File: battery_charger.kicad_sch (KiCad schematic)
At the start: 1 part, among them J8 Conn_01x04

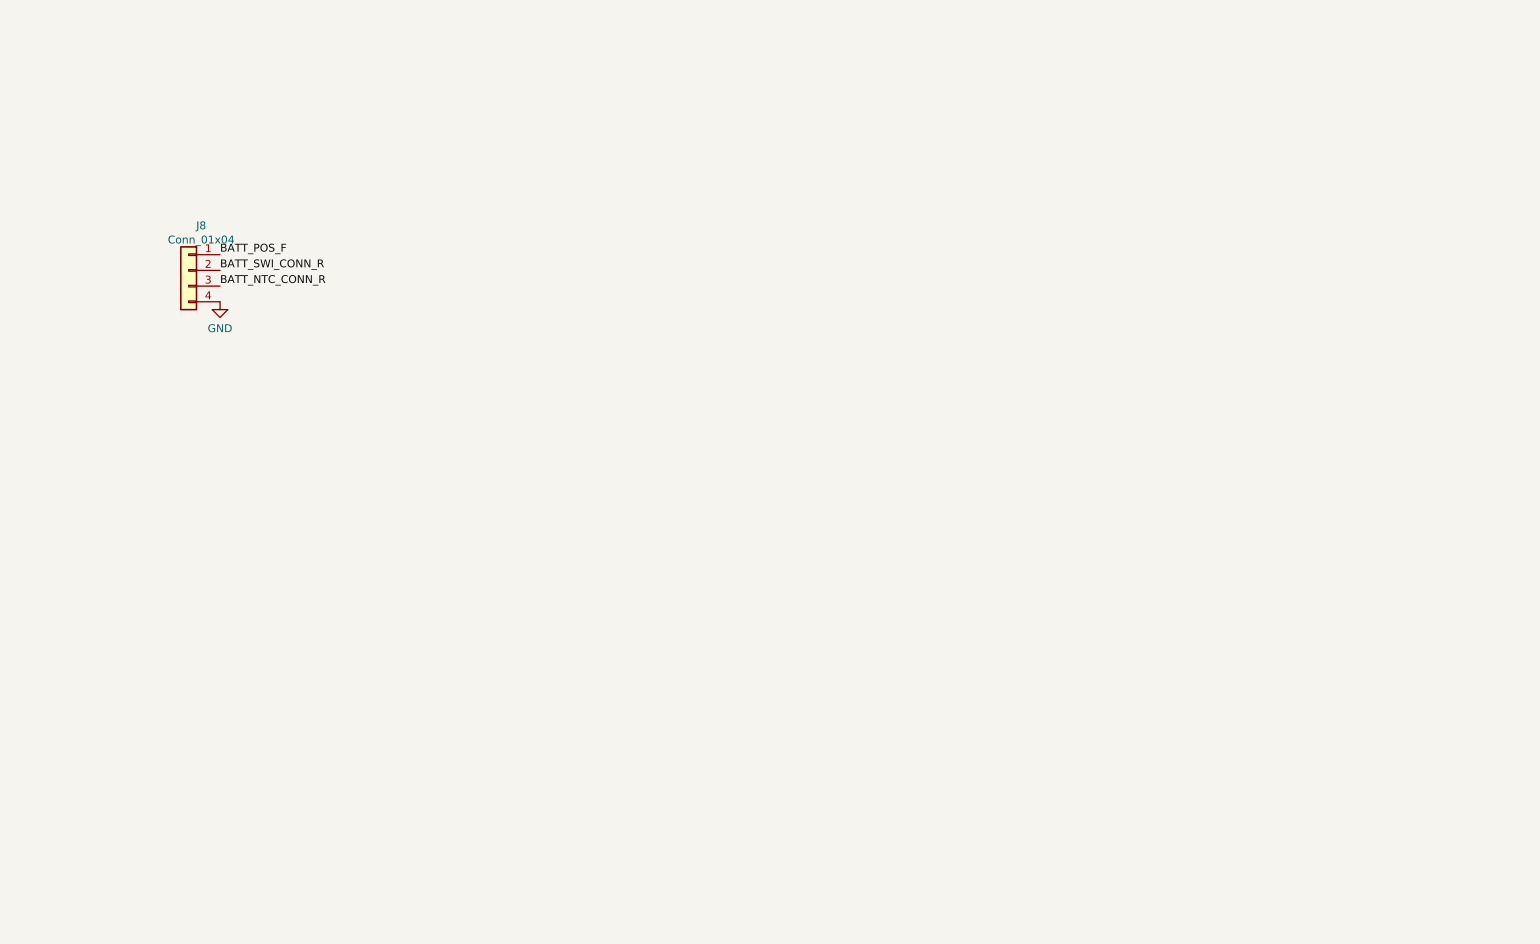
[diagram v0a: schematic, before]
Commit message: Add pinouts for dock connector; rearrange LCD backlight driver; copy the bq25895 schematic from SuperPower-RPi and add schottky to support 3.1A output on PMID.
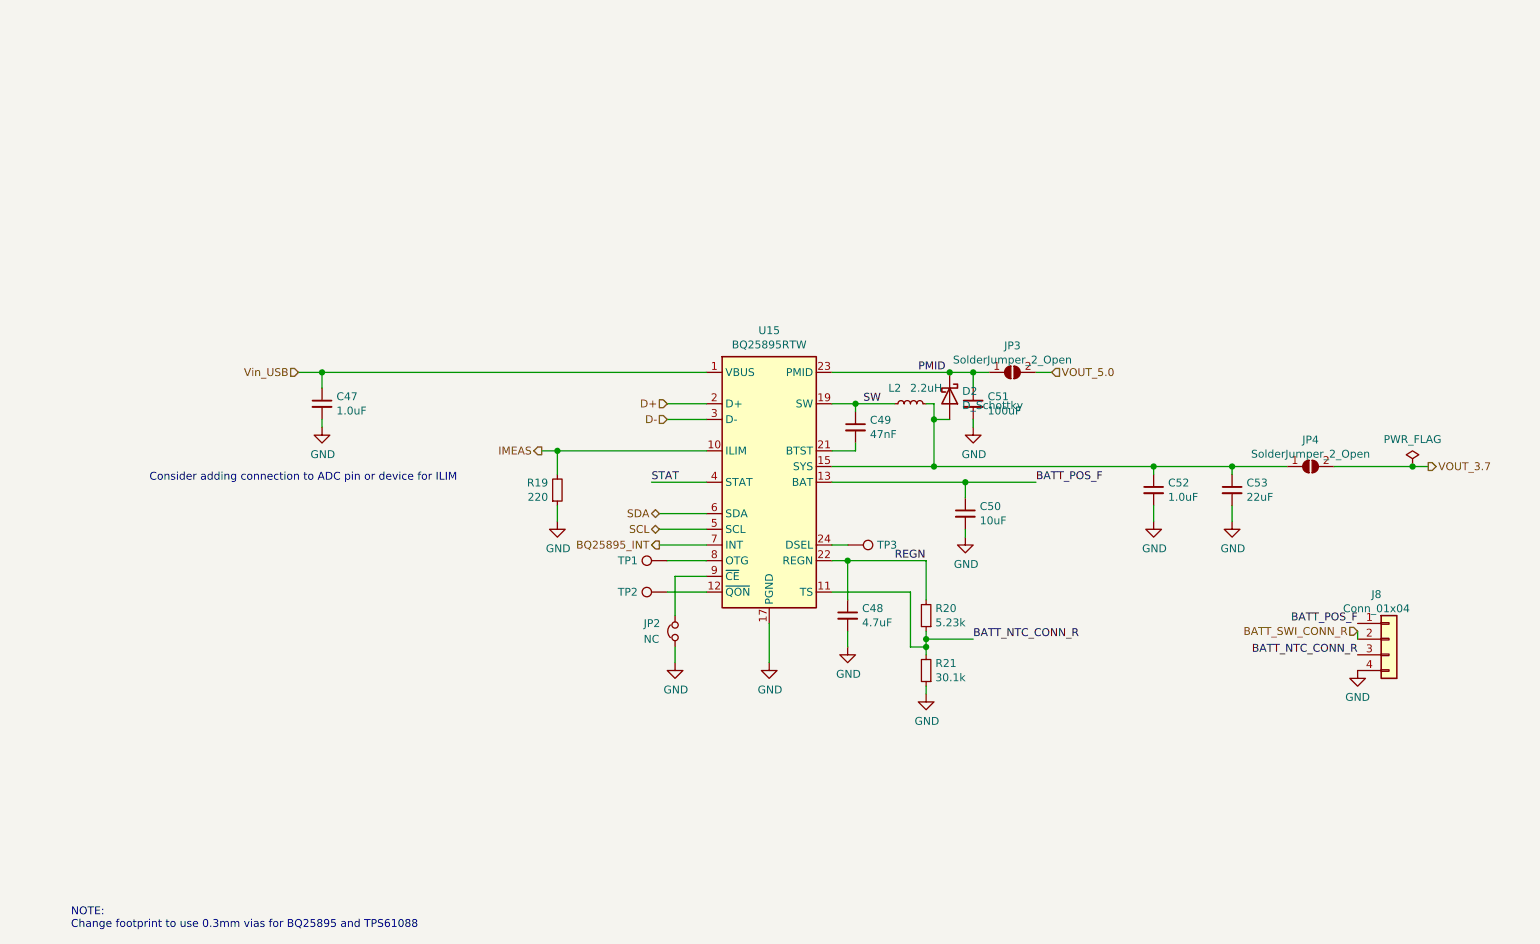
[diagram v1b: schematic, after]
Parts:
- added C47, C52: 1.0uF, Capacitor_SMD:C_0402_1005Metric, symbol Device:C_Small
- added C48: 4.7uF, Capacitor_SMD:C_0603_1608Metric, symbol Device:C_Small
- added C49: 47nF, Capacitor_SMD:C_0402_1005Metric, symbol Device:C_Small
- added C50: 10uF, Capacitor_SMD:C_0603_1608Metric, symbol Device:C_Small
- added C51: 100uF, Capacitor_SMD:C_1206_3216Metric, symbol Device:C_Small
- added C53: 22uF, Capacitor_SMD:C_0805_2012Metric, symbol Device:C_Small
- added D2: D_Schottky, footprints:NSR10F20NXT5G, symbol Device:D_Schottky
- added JP2: NC, Jumper:SolderJumper-2_P1.3mm_Bridged_RoundedPad1.0x1.5mm, symbol Device:Jumper_NC_Small
- added JP3, JP4: SolderJumper_2_Open, Jumper:SolderJumper-2_P1.3mm_Open_Pad1.0x1.5mm, symbol Jumper:SolderJumper_2_Open
- added L2: 2.2uH, Inductor_SMD:L_1008_2520Metric, symbol Device:L_Small
- added R19: 220, Resistor_SMD:R_0402_1005Metric, symbol Device:R_Small
- added R20: 5.23k, Resistor_SMD:R_0402_1005Metric, symbol Device:R_Small
- added R21: 30.1k, Resistor_SMD:R_0402_1005Metric, symbol Device:R_Small
- added TP1, TP2, TP3: DNP, TestPoint:TestPoint_Pad_1.0x1.0mm, symbol Connector:TestPoint
- added U15: BQ25895RTW, footprints:Texas_S-PWQFN-N24_EP2.7x2.7mm_ThermalVias, symbol Battery_Management:BQ25895RTW
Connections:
- net BATT_NTC_CONN_R: now also R20.1, R21.2, U15.11 (TS)
- net BATT_POS_F: now also C50.1, U15.13 (BAT), U15.14 (BAT)
- net GND: now also C47.2, C48.2, C50.2, C51.2, C52.2, C53.2, JP2.1, R19.1, R21.1, U15.17 (PGND), U15.18 (PGND), U15.25 (PGND)
- new net: C52.1, C53.1, D2.2 (A), JP4.1 (A), L2.2, U15.15 (SYS), U15.16 (SYS)
- new net: C49.2, U15.21 (BTST)
- new net: TP2.1, U15.12 (~QON)
- new net: TP3.1, U15.24 (DSEL)
- new net: TP1.1, U15.8 (OTG)
- new net: JP2.2, U15.9 (~CE)
- new net BQ25895_INT: U15.7 (INT)
- new net D+: U15.2 (D+)
- new net D-: U15.3 (D-)
- new net IMEAS: R19.2, U15.10 (ILIM)
- new net PMID: C51.1, D2.1 (K), JP3.1 (A), U15.23 (PMID)
- new net REGN: C48.1, R20.2, U15.22 (REGN)
- new net SCL: U15.5 (SCL)
- new net SDA: U15.6 (SDA)
- new net STAT: U15.4 (STAT)
- new net SW: C49.1, L2.1, U15.19 (SW), U15.20 (SW)
- new net VOUT_3.7: JP4.2 (B)
- new net VOUT_5.0: JP3.2 (B)
- new net Vin_USB: C47.1, U15.1 (VBUS)
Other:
- note added: "Consider adding connection to ADC pin or device for ILIM"
- note added: "NOTE: Change footprint to use 0.3mm vias for BQ25895 and TPS61088"
- moved on the sheet: J8

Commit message: Switch some footprints to minimize BOM costs. Cache a bunch more datasheets and documentation
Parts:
- C50: footprint Capacitor_SMD:C_0603_1608Metric -> Capacitor_SMD:C_0402_1005Metric
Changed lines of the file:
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@@
       (effects (font (size 1.27 1.27)) (justify left))
     )
-    (property "Footprint" "Capacitor_SMD:C_0603_1608Metric" (id 2) (at 175.26 100.33 0)
+    (property "Footprint" "Capacitor_SMD:C_0402_1005Metric" (id 2) (at 175.26 100.33 0)
       (effects (font (size 1.27 1.27)) hide)
     )

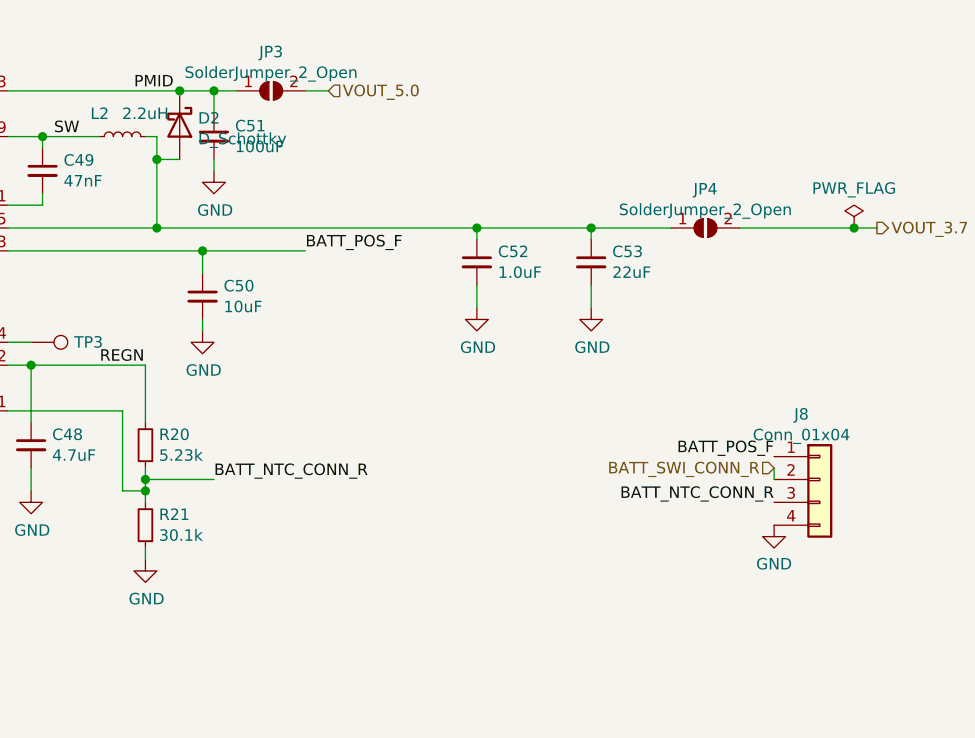
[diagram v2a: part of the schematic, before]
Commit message: WIP: add 2230 NVMe drive footprint
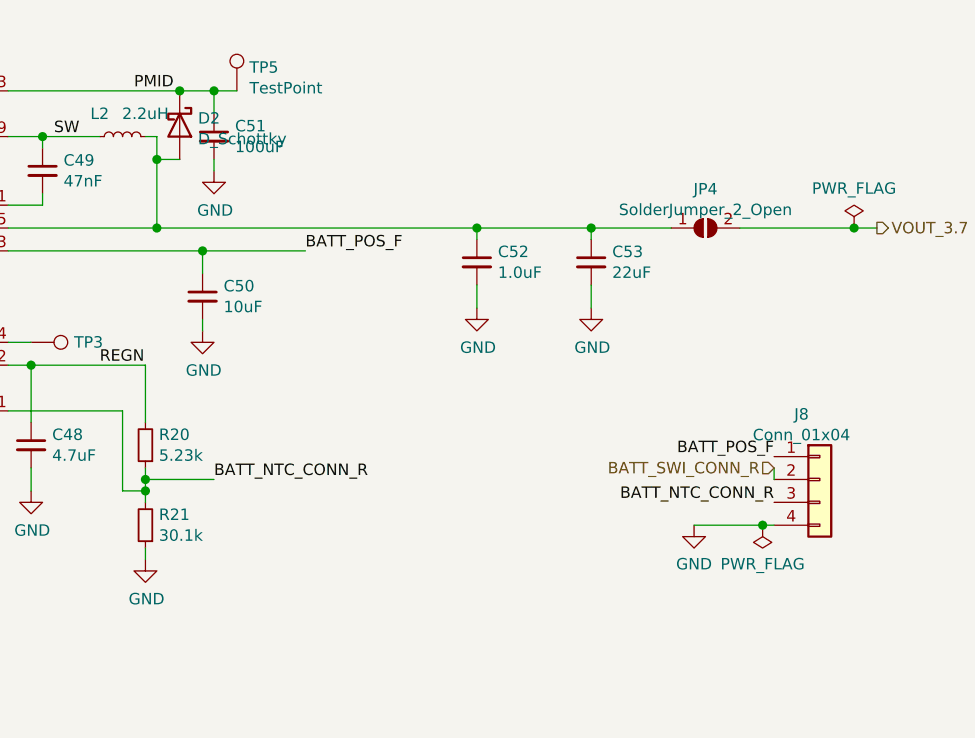
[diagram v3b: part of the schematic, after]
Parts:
- removed JP3: SolderJumper_2_Open, Jumper:SolderJumper-2_P1.3mm_Open_Pad1.0x1.5mm, symbol Jumper:SolderJumper_2_Open
- added TP5: TestPoint, symbol Connector:TestPoint
- JP2: footprint Jumper:SolderJumper-2_P1.3mm_Bridged_RoundedPad1.0x1.5mm -> Resistor_SMD:R_0402_1005Metric
- JP4: footprint Jumper:SolderJumper-2_P1.3mm_Open_Pad1.0x1.5mm -> Resistor_SMD:R_0402_1005Metric
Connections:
- net PMID: now also TP5.1
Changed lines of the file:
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@@
   (junction (at 205.74 92.71) (diameter 1.016) (color 0 0 0 0))
   (junction (at 218.44 92.71) (diameter 1.016) (color 0 0 0 0))
+  (junction (at 237.49 125.73) (diameter 1.016) (color 0 0 0 0))
   (junction (at 247.65 92.71) (diameter 1.016) (color 0 0 0 0))
   (wire (pts (xy 67.31 77.47) (xy 71.12 77.47))
@@
     (stroke (width 0) (type solid) (color 0 0 0 0))
   )
-  (wire (pts (xy 186.69 77.47) (xy 189.23 77.47))
-    (stroke (width 0) (type solid) (color 0 0 0 0))
-  )
   (wire (pts (xy 205.74 92.71) (xy 218.44 92.71))
     (stroke (width 0) (type solid) (color 0 0 0 0))
@@
     (stroke (width 0) (type solid) (color 0 0 0 0))
   )
+  (wire (pts (xy 229.87 125.73) (xy 237.49 125.73))
+    (stroke (width 0) (type solid) (color 0 0 0 0))
+  )
   (wire (pts (xy 234.95 92.71) (xy 247.65 92.71))
+    (stroke (width 0) (type solid) (color 0 0 0 0))
+  )
+  (wire (pts (xy 237.49 125.73) (xy 238.76 125.73))
     (stroke (width 0) (type solid) (color 0 0 0 0))
   )
@@
   (hierarchical_label "D-" (shape input) (at 127 85.09 180)
     (effects (font (size 1.27 1.27)) (justify right))
-  )
-  (hierarchical_label "VOUT_5.0" (shape input) (at 189.23 77.47 0)
-    (effects (font (size 1.27 1.27)) (justify left))
   )
   (hierarchical_label "BATT_SWI_CONN_R" (shape input) (at 238.76 119.38 180)
@@
     (pin "2")
   )
+  (symbol (lib_id "power:PWR_FLAG") (at 237.49 125.73 180) (unit 1)
+    (in_bom yes) (on_board yes) (fields_autoplaced)
+    (property "Reference" "#FLG0101" (id 0) (at 237.49 127.635 0)
+      (effects (font (size 1.27 1.27)) hide)
+    )
+    (property "Value" "PWR_FLAG" (id 1) (at 237.49 130.0544 0))
+    (property "Footprint" "" (id 2) (at 237.49 125.73 0)
+      (effects (font (size 1.27 1.27)) hide)
+    )
+    (property "Datasheet" "~" (id 3) (at 237.49 125.73 0)
+      (effects (font (size 1.27 1.27)) hide)
+    )
+    (pin "1")
+  )
   (symbol (lib_id "power:PWR_FLAG") (at 247.65 92.71 0) (unit 1)
     (in_bom yes) (on_board yes)
@@
     (pin "1")
   )
+  (symbol (lib_id "Connector:TestPoint") (at 179.07 77.47 0) (unit 1)
+    (in_bom yes) (on_board yes) (fields_autoplaced)
+    (property "Reference" "TP5" (id 0) (at 180.4671 74.8676 0)
+      (effects (font (size 1.27 1.27)) (justify left))
+    )
+    (property "Value" "TestPoint" (id 1) (at 180.4671 77.1663 0)
+      (effects (font (size 1.27 1.27)) (justify left))
+    )
+    (property "Footprint" "" (id 2) (at 184.15 77.47 0)
+      (effects (font (size 1.27 1.27)) hide)
+    )
+    (property "Datasheet" "~" (id 3) (at 184.15 77.47 0)
+      (effects (font (size 1.27 1.27)) hide)
+    )
+    (pin "1")
+  )
   (symbol (lib_id "power:GND") (at 71.12 86.36 0) (unit 1)
     (in_bom yes) (on_board yes)
@@
     (pin "1")
   )
-  (symbol (lib_id "power:GND") (at 238.76 125.73 0) (mirror y) (unit 1)
+  (symbol (lib_id "power:GND") (at 229.87 125.73 0) (mirror y) (unit 1)
     (in_bom yes) (on_board yes) (fields_autoplaced)
-    (property "Reference" "#PWR0124" (id 0) (at 238.76 132.08 0)
-      (effects (font (size 1.27 1.27)) hide)
-    )
-    (property "Value" "GND" (id 1) (at 238.76 130.0544 0))
-    (property "Footprint" "" (id 2) (at 238.76 125.73 0)
-      (effects (font (size 1.27 1.27)) hide)
-    )
-    (property "Datasheet" "" (id 3) (at 238.76 125.73 0)
+    (property "Reference" "#PWR0124" (id 0) (at 229.87 132.08 0)
+      (effects (font (size 1.27 1.27)) hide)
+    )
+    (property "Value" "GND" (id 1) (at 229.87 130.0544 0))
+    (property "Footprint" "" (id 2) (at 229.87 125.73 0)
+      (effects (font (size 1.27 1.27)) hide)
+    )
+    (property "Datasheet" "" (id 3) (at 229.87 125.73 0)
       (effects (font (size 1.27 1.27)) hide)
     )
@@
       (effects (font (size 1.27 1.27)) (justify right))
     )
-    (property "Footprint" "Jumper:SolderJumper-2_P1.3mm_Bridged_RoundedPad1.0x1.5mm" (id 2) (at 128.27 119.38 0)
+    (property "Footprint" "Resistor_SMD:R_0402_1005Metric" (id 2) (at 128.27 119.38 0)
       (effects (font (size 1.27 1.27)) hide)
     )
@@
     )
     (property "Mfg PN" "RMCF0402FT30K1‎" (id 6) (at 168.91 125.73 0)
-      (effects (font (size 1.27 1.27)) hide)
-    )
-    (pin "1")
-    (pin "2")
-  )
-  (symbol (lib_id "Jumper:SolderJumper_2_Open") (at 182.88 77.47 0) (unit 1)
-    (in_bom yes) (on_board yes) (fields_autoplaced)
-    (property "Reference" "JP3" (id 0) (at 182.88 73.1478 0))
-    (property "Value" "SolderJumper_2_Open" (id 1) (at 182.88 75.4465 0))
-    (property "Footprint" "Jumper:SolderJumper-2_P1.3mm_Open_Pad1.0x1.5mm" (id 2) (at 182.88 77.47 0)
-      (effects (font (size 1.27 1.27)) hide)
-    )
-    (property "Datasheet" "~" (id 3) (at 182.88 77.47 0)
       (effects (font (size 1.27 1.27)) hide)
     )
@@
     (property "Reference" "JP4" (id 0) (at 231.14 88.3878 0))
     (property "Value" "SolderJumper_2_Open" (id 1) (at 231.14 90.6865 0))
-    (property "Footprint" "Jumper:SolderJumper-2_P1.3mm_Open_Pad1.0x1.5mm" (id 2) (at 231.14 92.71 0)
-      (effects (font (size 1.27 1.27)) hide)
-    )
+    (property "Footprint" "Resistor_SMD:R_0402_1005Metric" (id 2) (at 231.14 92.71 0)
+      (effects (font (size 1.27 1.27)) hide)
+    )
